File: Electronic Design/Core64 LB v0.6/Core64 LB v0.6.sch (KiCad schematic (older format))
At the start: 14 parts, among them J12 TEENSY Cur. Mon., J4 PRG, U2 Teensy3.2

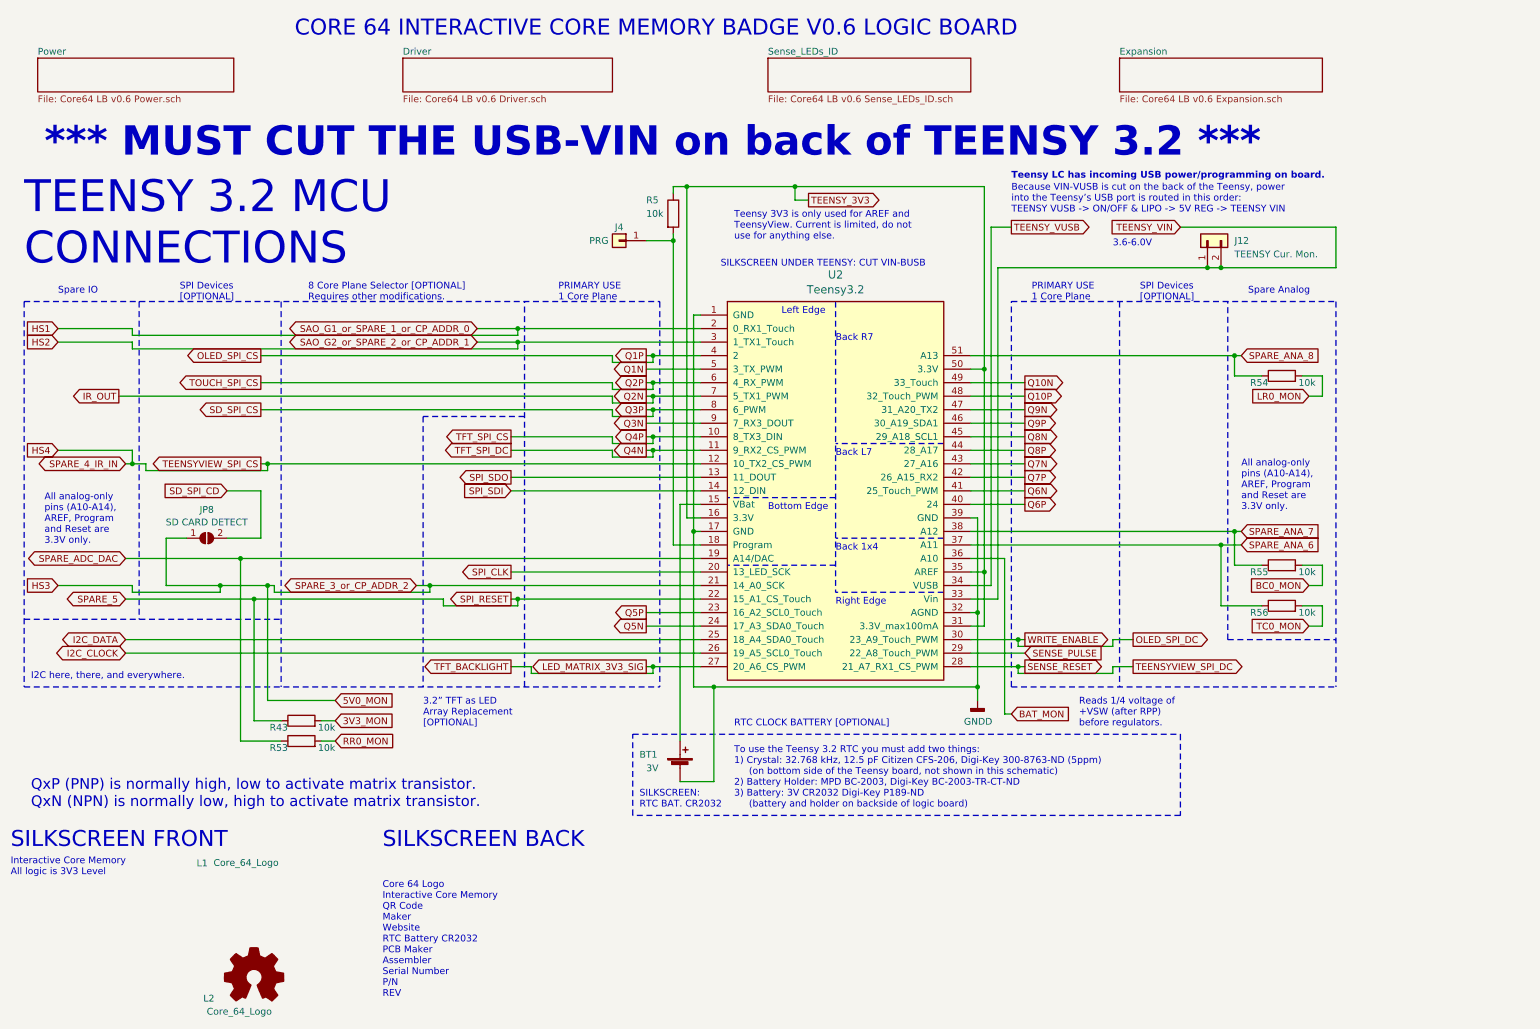
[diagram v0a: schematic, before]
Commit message: APPLY LOGIC BOARD V0.5 FIXES NEEDED TO BE V0.6 U1 silk screen should be placed by pin 1 not pin 7 Check J1 and J2 labels so J1 is on the left, like it is for the Core Board Remove Header for old LED Matrix, since is no longer needed and it is in the way. RTC Notes on schematic, must add THREE things, typo change from TWO. Below JP5 Teensy Charge Enable is a rogue "+" on the silk screen Left of R56 is a dead-end trace stub. Doesn't hurt anything but it's not right. 6.8 Ohm Core Current Limit Resistors can move to 5%. JP1/2 for OLED should be JP1/2 on the OLED silk screen, not JP3/4 Silk screen, left header row, swap SEN1 and SEN2 text so they match to S1 and S2 correctly on the inner perimeter. Move to larger logo and other text on the backside Update silk screen for all boards with P/Ns, bare board. Move top row of TFT LCD support down 0.55mm. Add 470 resistor to gate of core array enable to limit current. Change I2C pull-up resistors from 2.2K to 1.2K 20% (E12 series is most common, and values overlap) Remove two dead-end GND (BAT-) traces between/below Teensy 25/26, and over to QWIIC. Add I2C series resistors 68 Ohm at output of Teensy. Move the 470uF LED 5V0 capacitor, down to be between 5V0 Cur Mon and Teensy Charge enable jumpers, out of the way of the batteries. New stylus position is on left, so the 3V3 capacitor needs to move in a few mm to allow it to pass through. Provide thru-holes for alternate 3.3V and 5V bulk capacitor options. Propagation through sense logic chips was 200ns, reduce PU to 1K2 and remove inline 10Ks. Now 50ns. Voltage divider and other resistors, consolidated to 10K resistors. Keep the two 10K resistors on the 5V0 MON. Add a SJ in series to isolate from Hall Switches. Replace the inline 10K resistors in the all optional Voltage Monitoring lines with closed SJs instead. Clean-up all the horz/vert traces left from removing LED drive header and relocating the driver and 5V0 cap Part substitutions Data sheet updates
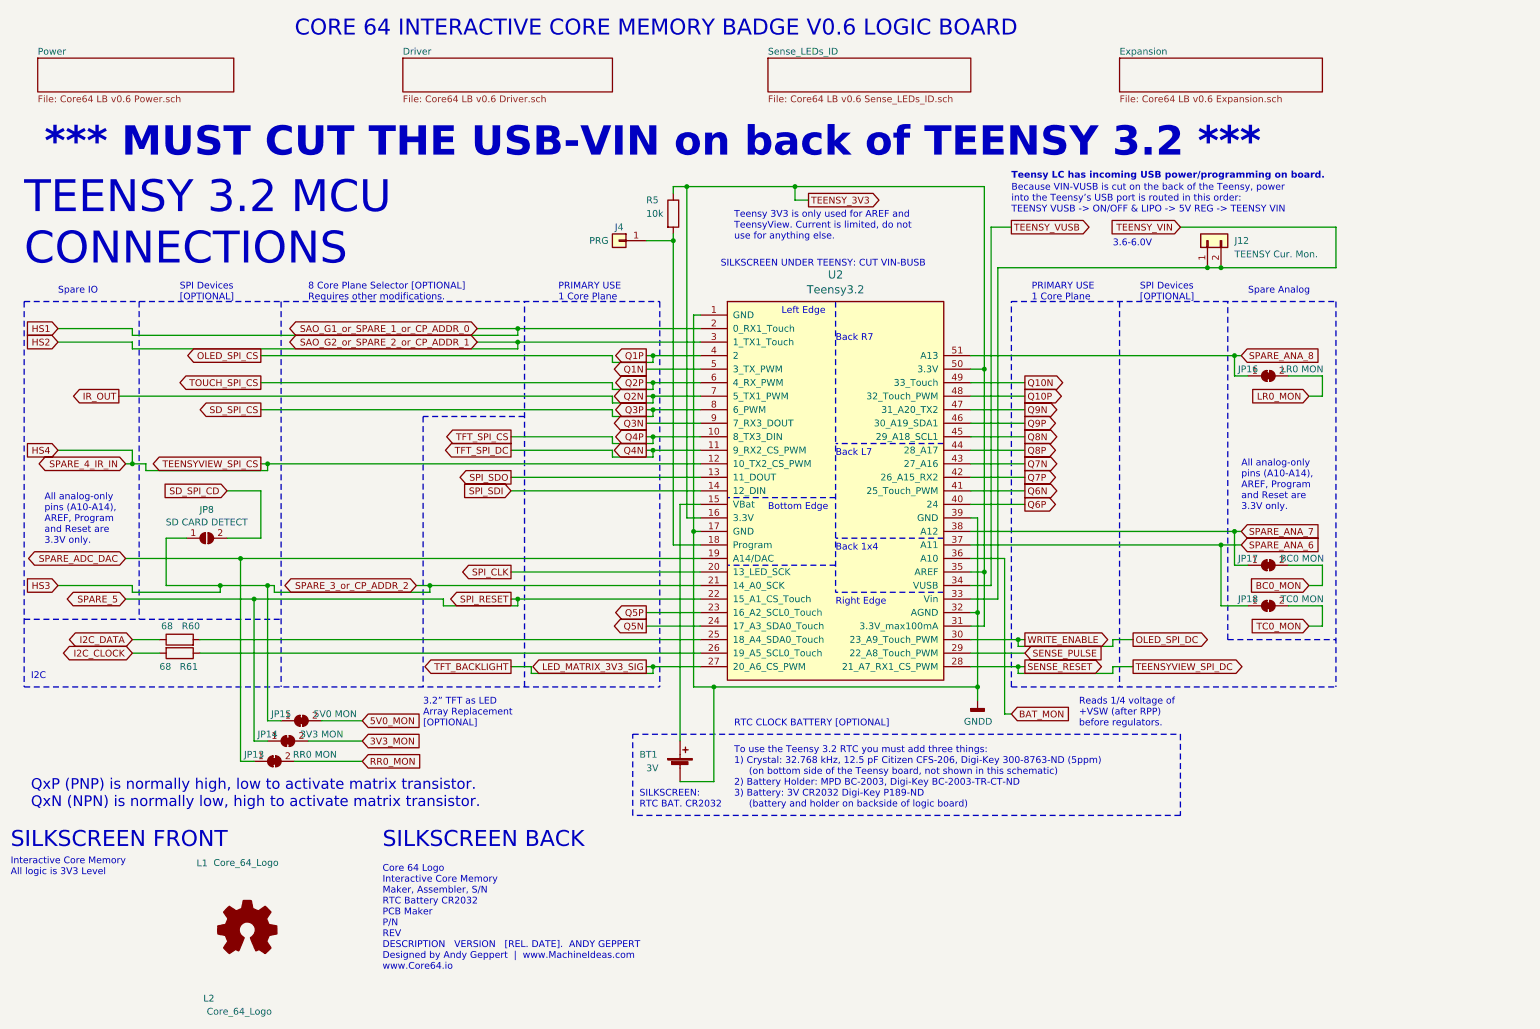
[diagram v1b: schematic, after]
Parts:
- removed R43, R53, R54, R55, R56: 10k, Resistor_SMD:R_0805_2012Metric, symbol Device:R
- added JP13: RR0 MON, Jumper:SolderJumper-2_P1.3mm_Bridged_Pad1.0x1.5mm, symbol Jumper:SolderJumper_2_Bridged
- added JP14: 3V3 MON, Jumper:SolderJumper-2_P1.3mm_Bridged_Pad1.0x1.5mm, symbol Jumper:SolderJumper_2_Bridged
- added JP15: 5V0 MON, Jumper:SolderJumper-2_P1.3mm_Bridged_Pad1.0x1.5mm, symbol Jumper:SolderJumper_2_Bridged
- added JP16: LR0 MON, Jumper:SolderJumper-2_P1.3mm_Bridged_Pad1.0x1.5mm, symbol Jumper:SolderJumper_2_Bridged
- added JP17: BC0 MON, Jumper:SolderJumper-2_P1.3mm_Bridged_Pad1.0x1.5mm, symbol Jumper:SolderJumper_2_Bridged
- added JP18: TC0 MON, Jumper:SolderJumper-2_P1.3mm_Bridged_Pad1.0x1.5mm, symbol Jumper:SolderJumper_2_Bridged
- added R60, R61: 68, Resistor_SMD:R_0805_2012Metric, symbol Device:R
- L2: footprint Core_Memory_8x8_Array:Core64_Logo -> Core_Memory_8x8_Array:Core64_Logo_9mm_tall
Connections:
- net 3V3_MON: now also JP14.2 (B)
- net 5V0_MON: now also JP15.2 (B); no longer JP8.1 (A), U2.21 (14_A0_SCK)
- net BC0_MON: now also JP17.2 (B)
- net I2C_CLOCK: now also R61.2; no longer U2.26 (19_A5_SCL0_Touch)
- net I2C_DATA: now also R60.1; no longer U2.25 (18_A4_SDA0_Touch)
- net LR0_MON: now also JP16.2 (B)
- net RR0_MON: now also JP13.2 (B)
- net SPARE_5: now also JP14.1 (A)
- net SPARE_ADC_DAC: now also JP13.1 (A)
- net SPARE_ANA_6: now also JP18.1 (A)
- net SPARE_ANA_7: now also JP17.1 (A)
- net SPARE_ANA_8: now also JP16.1 (A)
- net TC0_MON: now also JP18.2 (B)
- new net: R60.2, U2.25 (18_A4_SDA0_Touch)
- new net: R61.1, U2.26 (19_A5_SCL0_Touch)
- new net HS3: JP15.1 (A), JP8.1 (A), U2.21 (14_A0_SCK)
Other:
- note added: "Core 64 Logo\nInteractive Core Memory\nMaker, Assembler, S/N\nRTC Battery CR2032\nPCB Maker\nP/N\nREV\nDESCRIPTION VERSION [REL. DATE]. ANDY GEPPERT \nDesigned by Andy Geppert | www.MachineIdeas.com\nwww.Core64.io"
- note added: "I2C"
- note added: "To use the Teensy 3.2 RTC you must add three things:\n1) Crystal: 32.768 kHz, 12.5 pF Citizen CFS-206, Digi-Key 300-8763-ND (5ppm)\n (on bottom side of the Teensy board, not shown in this schematic)\n2) Battery Holder: MPD BC-2003, Digi-Key BC-2003-TR-CT-ND\n3) Battery: 3V CR2032 Digi-Key P189-ND\n (battery and holder on backside of logic board)\n"
- note removed: "Core 64 Logo\nInteractive Core Memory\nQR Code\nMaker\nWebsite\nRTC Battery CR2032\nPCB Maker\nAssembler\nSerial Number\nP/N\nREV"
- note removed: "I2C here, there, and everywhere."
- note removed: "To use the Teensy 3.2 RTC you must add two things:\n1) Crystal: 32.768 kHz, 12.5 pF Citizen CFS-206, Digi-Key 300-8763-ND (5ppm)\n (on bottom side of the Teensy board, not shown in this schematic)\n2) Battery Holder: MPD BC-2003, Digi-Key BC-2003-TR-CT-ND\n3) Battery: 3V CR2032 Digi-Key P189-ND\n (battery and holder on backside of logic board)\n"

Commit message: Revise LB V0.6, part substitutions, data sheet updates, clean up Ref. Des. to be in order and easier to find on the board in groups
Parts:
- BT1: Description (none) -> Battery Cell Holder; Insert? (none) -> No
- J11: renamed from J4; Insert? (none) -> No
- J12, JP13, JP14, JP15, JP16, JP17, JP18, JP8, L1, L2, L4: Insert? (none) -> No
- R47: renamed from R5; Description (none) -> RES 10K OHM; Insert? (none) -> Yes; Value_Modifier (none) -> 20%
- R48: renamed from R60; Description (none) -> RES 68 OHM; Insert? (none) -> Yes; Value_Modifier (none) -> 10%
- R49: renamed from R61; Description (none) -> RES 68 OHM; Insert? (none) -> Yes; Value_Modifier (none) -> 10%
- U8: renamed from U2; Description (none) -> TEENSY 3.2; Insert? (none) -> No
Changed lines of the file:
@@
 Sheet 1 5
 Title "Core 64 - Main Sheet Index"
-Date "2021-11-05"
+Date "2021-11-08"
 Rev "0.6"
 Comp "Concept and design by Andy Geppert @ www.MachineIdeas.com"
@@
 F 2 "Core_Memory_8x8_Array:Core64_Logo" H 1900 6850 50  0001 C CNN
 F 3 "" H 1900 6850 50  0001 C CNN
+F 4 "No" H 1900 6850 50  0001 C CNN "Insert?"
 	1    1900 6850
 	1    0    0    -1
@@
 F 2 "Core_Memory_8x8_Array:Core64_Logo_9mm_tall" H 1950 7850 50  0001 C CNN
 F 3 "" H 1950 7850 50  0001 C CNN
+F 4 "No" H 1950 7850 50  0001 C CNN "Insert?"
 	1    1950 7850
 	1    0    0    -1
@@
 $EndComp
 $Comp
-L Teensy:Teensy3.2 U2
+L Teensy:Teensy3.2 U8
 U 1 1 5F49143E
 P 6650 4050
-F 0 "U2" H 6650 5648 60  0000 C CNN
+F 0 "U8" H 6650 5648 60  0000 C CNN
 F 1 "Teensy3.2" H 6650 5538 60  0000 C CNN
 F 2 "Teensy:Teensy30_31_32_LC_SMD_SOCKETS" H 6650 3250 60  0001 C CNN
 F 3 "" H 6650 3250 60  0000 C CNN
+F 4 "No" H 6650 4050 50  0001 C CNN "Insert?"
+F 5 "TEENSY 3.2" H 6650 4050 50  0001 C CNN "Description"
 	1    6650 4050
 	1    0    0    -1
@@
 AR Path="/5E755787/5F73FDF3" Ref="R?"  Part="1"
 AR Path="/5E755AC8/5D2551FF/5F73FDF3" Ref="R?"  Part="1"
-AR Path="/5F73FDF3" Ref="R5"  Part="1"
-F 0 "R5" H 5250 2100 50  0000 L CNN
+AR Path="/5F73FDF3" Ref="R47"  Part="1"
+F 0 "R47" H 5250 2100 50  0000 L CNN
 F 1 "10k" H 5250 2000 50  0000 L CNN
 F 2 "Resistor_SMD:R_0805_2012Metric" V 5380 2000 50  0001 C CNN
 F 3 "~" H 5450 2000 50  0001 C CNN
+F 4 "RES 10K OHM" H 5450 2000 50  0001 C CNN "Description"
+F 5 "Yes" H 5450 2000 50  0001 C CNN "Insert?"
+F 6 "20%" H 5450 2000 50  0001 C CNN "Value_Modifier"
 	1    5450 2000
 	1    0    0    -1
@@
 AR Path="/5E7548ED/5F7507F8" Ref="J?"  Part="1"
 AR Path="/5E755AC8/5D254AE8/5F7507F8" Ref="J?"  Part="1"
-AR Path="/5F7507F8" Ref="J4"  Part="1"
-F 0 "J4" H 5050 2300 50  0000 C CNN
+AR Path="/5F7507F8" Ref="J11"  Part="1"
+F 0 "J11" H 5050 2300 50  0000 C CNN
 F 1 "PRG" H 5200 2200 50  0000 C CNN
 F 2 "Connector_PinSocket_2.54mm:PinSocket_1x01_P2.54mm_Vertical" H 5050 2200 50  0001 C CNN
 F 3 "~" H 5050 2200 50  0001 C CNN
+F 4 "No" H 5050 2200 50  0001 C CNN "Insert?"
 	1    5050 2200
 	-1   0    0    -1
@@
 F 2 "Battery:BatteryHolder_MPD_BC2003_1x2032" V 5500 6160 50  0001 C CNN
 F 3 "~" V 5500 6160 50  0001 C CNN
+F 4 "No" H 5500 6100 50  0001 C CNN "Insert?"
+F 5 "Battery Cell Holder" H 5500 6100 50  0001 C CNN "Description"
 	1    5500 6100
 	1    0    0    -1
@@
 F 2 "Connector_PinSocket_2.54mm:PinSocket_1x02_P2.54mm_Vertical" H 9400 2200 50  0001 C CNN
 F 3 "~" H 9400 2200 50  0001 C CNN
+F 4 "No" H 9400 2200 50  0001 C CNN "Insert?"
 	1    9400 2200
 	0    -1   -1   0
@@
 F 2 "Symbol:OSHW-Logo2_7.3x6mm_SilkScreen" H 2300 7300 50  0001 C CNN
 F 3 "~" H 2300 7300 50  0001 C CNN
+F 4 "No" H 2300 7300 50  0001 C CNN "Insert?"
 	1    2300 7300
 	1    0    0    -1
@@
 F 2 "Jumper:SolderJumper-2_P1.3mm_Open_RoundedPad1.0x1.5mm" H 2000 4400 50  0001 C CNN
 F 3 "~" H 2000 4400 50  0001 C CNN
+F 4 "No" H 2000 4400 50  0001 C CNN "Insert?"
 	1    2000 4400
 	1    0    0    -1
@@
 AR Path="/5E755787/61998E01" Ref="R?"  Part="1"
 AR Path="/5E755AC8/5D2551FF/61998E01" Ref="R?"  Part="1"
-AR Path="/61998E01" Ref="R60"  Part="1"
+AR Path="/61998E01" Ref="R48"  Part="1"
 AR Path="/5EA63449/61998E01" Ref="R?"  Part="1"
-F 0 "R60" V 1900 5000 50  0000 L CNN
+F 0 "R48" V 1900 5000 50  0000 L CNN
 F 1 "68" V 1900 5200 50  0000 L CNN
 F 2 "Resistor_SMD:R_0805_2012Metric" V 1730 5150 50  0001 C CNN
 F 3 "~" H 1800 5150 50  0001 C CNN
+F 4 "RES 68 OHM" H 1800 5150 50  0001 C CNN "Description"
+F 5 "10%" H 1800 5150 50  0001 C CNN "Value_Modifier"
+F 6 "Yes" H 1800 5150 50  0001 C CNN "Insert?"
 	1    1800 5150
 	0    -1   -1   0
@@
 AR Path="/5E755787/61998E07" Ref="R?"  Part="1"
 AR Path="/5E755AC8/5D2551FF/61998E07" Ref="R?"  Part="1"
-AR Path="/61998E07" Ref="R61"  Part="1"
+AR Path="/61998E07" Ref="R49"  Part="1"
 AR Path="/5EA63449/61998E07" Ref="R?"  Part="1"
-F 0 "R61" V 1900 5250 50  0000 L CNN
+F 0 "R49" V 1900 5250 50  0000 L CNN
 F 1 "68" V 1900 5100 50  0000 L CNN
 F 2 "Resistor_SMD:R_0805_2012Metric" V 1730 5250 50  0001 C CNN
 F 3 "~" H 1800 5250 50  0001 C CNN
+F 4 "RES 68 OHM" H 1800 5250 50  0001 C CNN "Description"
+F 5 "10%" H 1800 5250 50  0001 C CNN "Value_Modifier"
+F 6 "Yes" H 1800 5250 50  0001 C CNN "Insert?"
 	1    1800 5250
 	0    1    1    0
@@
 F 2 "Jumper:SolderJumper-2_P1.3mm_Bridged_Pad1.0x1.5mm" H 2700 5750 50  0001 C CNN
 F 3 "~" H 2700 5750 50  0001 C CNN
+F 4 "No" H 2700 5750 50  0001 C CNN "Insert?"
 	1    2700 5750
 	1    0    0    -1
@@
 F 2 "Jumper:SolderJumper-2_P1.3mm_Bridged_Pad1.0x1.5mm" H 2600 5900 50  0001 C CNN
 F 3 "~" H 2600 5900 50  0001 C CNN
+F 4 "No" H 2600 5900 50  0001 C CNN "Insert?"
 	1    2600 5900
 	1    0    0    -1
@@
 F 2 "Jumper:SolderJumper-2_P1.3mm_Bridged_Pad1.0x1.5mm" H 2500 6050 50  0001 C CNN
 F 3 "~" H 2500 6050 50  0001 C CNN
+F 4 "No" H 2500 6050 50  0001 C CNN "Insert?"
 	1    2500 6050
 	1    0    0    -1
@@
 F 2 "Jumper:SolderJumper-2_P1.3mm_Bridged_Pad1.0x1.5mm" H 9850 3200 50  0001 C CNN
 F 3 "~" H 9850 3200 50  0001 C CNN
+F 4 "No" H 9850 3200 50  0001 C CNN "Insert?"
 	1    9850 3200
 	1    0    0    -1
@@
 F 2 "Jumper:SolderJumper-2_P1.3mm_Bridged_Pad1.0x1.5mm" H 9850 4600 50  0001 C CNN
 F 3 "~" H 9850 4600 50  0001 C CNN
+F 4 "No" H 9850 4600 50  0001 C CNN "Insert?"
 	1    9850 4600
 	1    0    0    -1
@@
 F 2 "Jumper:SolderJumper-2_P1.3mm_Bridged_Pad1.0x1.5mm" H 9850 4900 50  0001 C CNN
 F 3 "~" H 9850 4900 50  0001 C CNN
+F 4 "No" H 9850 4900 50  0001 C CNN "Insert?"
 	1    9850 4900
 	1    0    0    -1

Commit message: Refine LB v0.6 layout, KiCAD BOM updates, review schematic and PCB for release
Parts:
- BT1: Description Battery Cell Holder -> Battery Cell Holder, CR2032; MPN (none) -> MPD BC-2003
- renumbered J11 to J13, J12 to J14, JP14 to JP10, JP13 to JP11, JP16 to JP12, JP17 to JP13, JP18 to JP14, JP15 to JP9, U8 to U7
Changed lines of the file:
@@
 Sheet 1 5
 Title "Core 64 - Main Sheet Index"
-Date "2021-11-08"
+Date "2021-11-09"
 Rev "0.6"
 Comp "Concept and design by Andy Geppert @ www.MachineIdeas.com"
 Comment1 "Visit www.Core64.io for information on assembly and optional features."
-Comment2 "WIP"
+Comment2 "As released"
 Comment3 ""
 Comment4 "All non-polarized capacitors are X7R or X5R ceramic unless otherwise noted."
@@
 $EndComp
 $Comp
-L Teensy:Teensy3.2 U8
+L Teensy:Teensy3.2 U7
 U 1 1 5F49143E
 P 6650 4050
-F 0 "U8" H 6650 5648 60  0000 C CNN
+F 0 "U7" H 6650 5648 60  0000 C CNN
 F 1 "Teensy3.2" H 6650 5538 60  0000 C CNN
 F 2 "Teensy:Teensy30_31_32_LC_SMD_SOCKETS" H 6650 3250 60  0001 C CNN
@@
 AR Path="/5E7548ED/5F7507F8" Ref="J?"  Part="1"
 AR Path="/5E755AC8/5D254AE8/5F7507F8" Ref="J?"  Part="1"
-AR Path="/5F7507F8" Ref="J11"  Part="1"
-F 0 "J11" H 5050 2300 50  0000 C CNN
+AR Path="/5F7507F8" Ref="J13"  Part="1"
+F 0 "J13" H 5050 2300 50  0000 C CNN
 F 1 "PRG" H 5200 2200 50  0000 C CNN
 F 2 "Connector_PinSocket_2.54mm:PinSocket_1x01_P2.54mm_Vertical" H 5050 2200 50  0001 C CNN
@@
 F 3 "~" V 5500 6160 50  0001 C CNN
 F 4 "No" H 5500 6100 50  0001 C CNN "Insert?"
-F 5 "Battery Cell Holder" H 5500 6100 50  0001 C CNN "Description"
+F 5 "Battery Cell Holder, CR2032" H 5500 6100 50  0001 C CNN "Description"
+F 6 "MPD BC-2003" H 5500 6100 50  0001 C CNN "MPN"
 	1    5500 6100
 	1    0    0    -1
@@
 P 9400 2200
 AR Path="/5E7548ED/5F9FB501" Ref="J?"  Part="1"
-AR Path="/5F9FB501" Ref="J12"  Part="1"
-F 0 "J12" V 9400 2000 50  0000 R CNN
+AR Path="/5F9FB501" Ref="J14"  Part="1"
+F 0 "J14" V 9400 2000 50  0000 R CNN
 F 1 "TEENSY Cur. Mon." V 9300 2000 50  0000 R CNN
 F 2 "Connector_PinSocket_2.54mm:PinSocket_1x02_P2.54mm_Vertical" H 9400 2200 50  0001 C CNN
@@
 P 2700 5750
 AR Path="/5E7548ED/61B618D6" Ref="JP?"  Part="1"
-AR Path="/61B618D6" Ref="JP15"  Part="1"
-F 0 "JP15" H 2550 5800 50  0000 C CNN
+AR Path="/61B618D6" Ref="JP9"  Part="1"
+F 0 "JP9" H 2550 5800 50  0000 C CNN
 F 1 "5V0 MON" H 2950 5800 50  0000 C CNN
 F 2 "Jumper:SolderJumper-2_P1.3mm_Bridged_Pad1.0x1.5mm" H 2700 5750 50  0001 C CNN
@@
 P 2600 5900
 AR Path="/5E7548ED/61BC2A0E" Ref="JP?"  Part="1"
-AR Path="/61BC2A0E" Ref="JP14"  Part="1"
-F 0 "JP14" H 2450 5950 50  0000 C CNN
+AR Path="/61BC2A0E" Ref="JP10"  Part="1"
+F 0 "JP10" H 2450 5950 50  0000 C CNN
 F 1 "3V3 MON" H 2850 5950 50  0000 C CNN
 F 2 "Jumper:SolderJumper-2_P1.3mm_Bridged_Pad1.0x1.5mm" H 2600 5900 50  0001 C CNN
@@
 P 2500 6050
 AR Path="/5E7548ED/61BC2DF2" Ref="JP?"  Part="1"
-AR Path="/61BC2DF2" Ref="JP13"  Part="1"
-F 0 "JP13" H 2350 6100 50  0000 C CNN
+AR Path="/61BC2DF2" Ref="JP11"  Part="1"
+F 0 "JP11" H 2350 6100 50  0000 C CNN
 F 1 "RR0 MON" H 2800 6100 50  0000 C CNN
 F 2 "Jumper:SolderJumper-2_P1.3mm_Bridged_Pad1.0x1.5mm" H 2500 6050 50  0001 C CNN
@@
 P 9850 3200
 AR Path="/5E7548ED/61C35ED3" Ref="JP?"  Part="1"
-AR Path="/61C35ED3" Ref="JP16"  Part="1"
-F 0 "JP16" H 9700 3250 50  0000 C CNN
+AR Path="/61C35ED3" Ref="JP12"  Part="1"
+F 0 "JP12" H 9700 3250 50  0000 C CNN
 F 1 "LR0 MON" H 10100 3250 50  0000 C CNN
 F 2 "Jumper:SolderJumper-2_P1.3mm_Bridged_Pad1.0x1.5mm" H 9850 3200 50  0001 C CNN
@@
 P 9850 4600
 AR Path="/5E7548ED/61C4788B" Ref="JP?"  Part="1"
-AR Path="/61C4788B" Ref="JP17"  Part="1"
-F 0 "JP17" H 9700 4650 50  0000 C CNN
+AR Path="/61C4788B" Ref="JP13"  Part="1"
+F 0 "JP13" H 9700 4650 50  0000 C CNN
 F 1 "BC0 MON" H 10100 4650 50  0000 C CNN
 F 2 "Jumper:SolderJumper-2_P1.3mm_Bridged_Pad1.0x1.5mm" H 9850 4600 50  0001 C CNN
@@
 P 9850 4900
 AR Path="/5E7548ED/61C5666B" Ref="JP?"  Part="1"
-AR Path="/61C5666B" Ref="JP18"  Part="1"
-F 0 "JP18" H 9700 4950 50  0000 C CNN
+AR Path="/61C5666B" Ref="JP14"  Part="1"
+F 0 "JP14" H 9700 4950 50  0000 C CNN
 F 1 "TC0 MON" H 10100 4950 50  0000 C CNN
 F 2 "Jumper:SolderJumper-2_P1.3mm_Bridged_Pad1.0x1.5mm" H 9850 4900 50  0001 C CNN
